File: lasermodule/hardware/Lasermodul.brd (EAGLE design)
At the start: 96 parts, among them IC1 MEGA8-AI

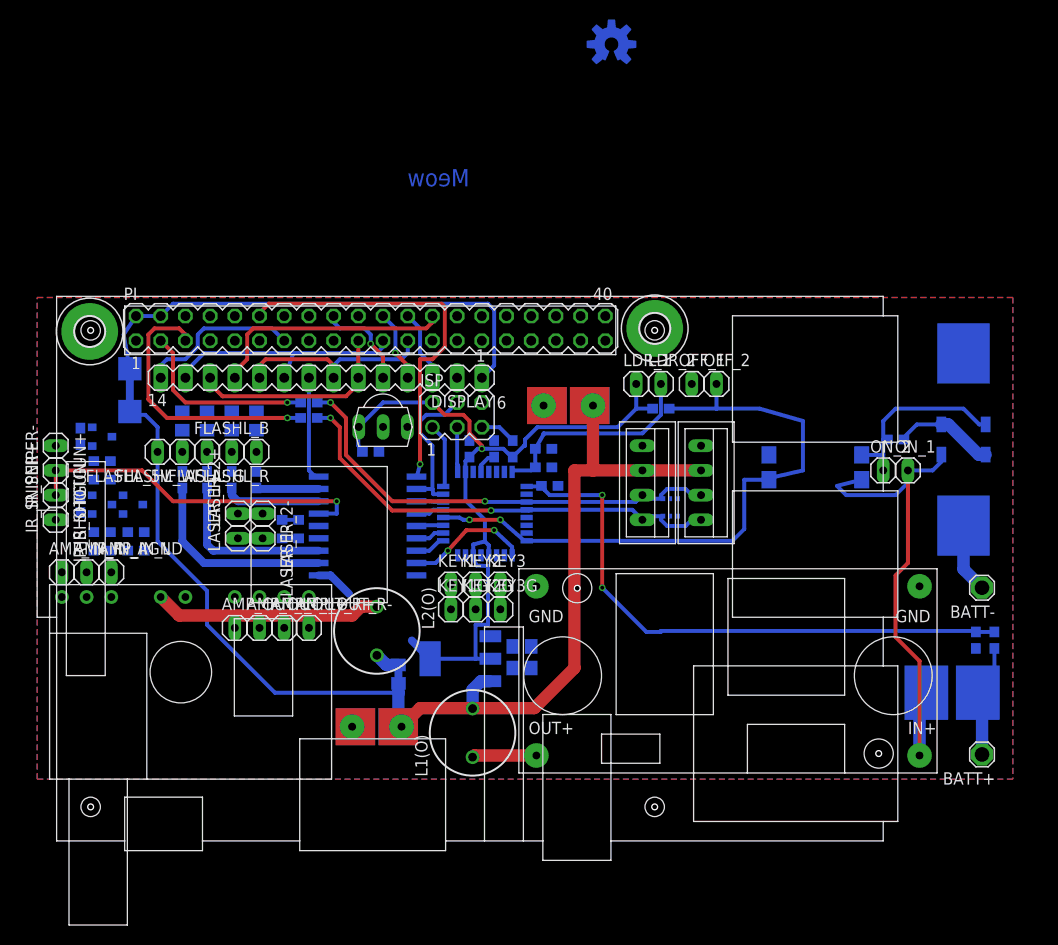
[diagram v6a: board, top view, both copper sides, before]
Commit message: routing and a bit case design
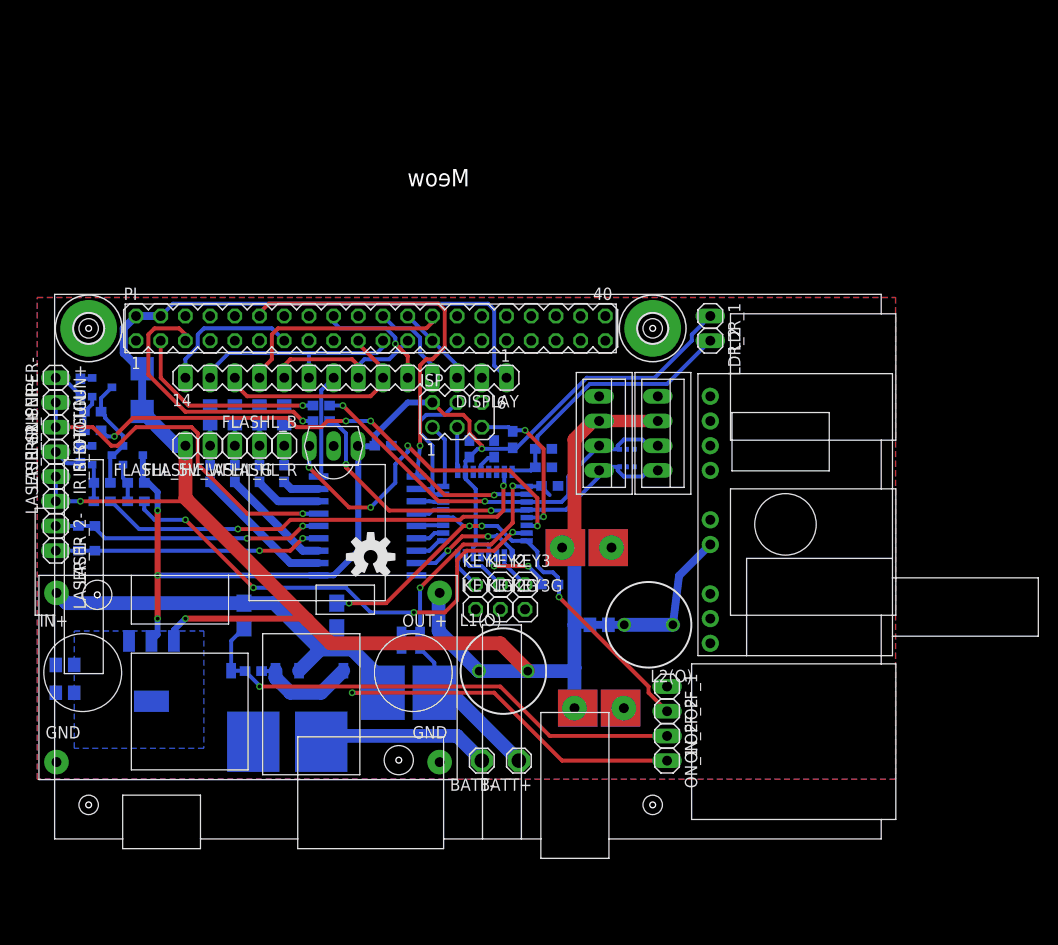
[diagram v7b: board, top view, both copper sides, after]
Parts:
- removed AMP_IN_AGND, AMP_IN_L, AMP_IN_R, AMP_OUT_L+, AMP_OUT_L-, AMP_OUT_R+, AMP_OUT_R-: (no value), wz:PIN-HEADER-1
- KEY1, KEY1G, KEY2, KEY2G, KEY3, KEY3G: device wz:PIN-HEADER-1 -> wz:PIN-HEADER-1_SMALL
- LOGO1: device wz:OSHW-LOGO-M -> SparkFun-Aesthetics:OSHW-LOGO-M
- moved ON 80.9 mm to (22.2, 6.35), turned to 180 degrees
- moved U$2 74.5 mm to (34.3, 46.4)
- moved R9 70.2 mm to (22.2, 11.1)
- moved REV 69.7 mm to (29.2, 6.35)
- moved U$4 67.1 mm to (67.9, 12.7), turned to 90 degrees
- moved R4 59.1 mm to (39.4, 14.3)
- moved R5 59.1 mm to (37.5, 14.3)
- moved LOGO1 58.2 mm to (34.3, 22.9)
- moved OK1 56.1 mm to (26.0, 16.8), turned to 270 degrees
- moved 2A_4A 55.9 mm to (41.9, 8.89)
- moved BATT- 54.4 mm to (45.7, 1.91)
- moved BATT+ 47.6 mm to (49.5, 1.91)
- moved C11 47.1 mm to (2.86, 8.89), turned to 0 degrees
- moved C2 47.0 mm to (2.86, 11.7), turned to 0 degrees
- moved ON_1 38.8 mm to (64.8, 1.91), turned to 270 degrees
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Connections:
- net +5V: now also C12.+A, C12.+B, C12.+C, C3.+A, C3.+B, C3.+C; no longer C12.1, C12.1B, C3.1, C3.1B
- net AMP_IN_AGND: no longer AMP_IN_AGND.1
- net AMP_IN_L: no longer AMP_IN_L.1
- net AMP_IN_R: no longer AMP_IN_R.1
- net AMP_OUT_L+: no longer AMP_OUT_L+.1
- net AMP_OUT_L-: no longer AMP_OUT_L-.1
- net AMP_OUT_R+: no longer AMP_OUT_R+.1
- net AMP_OUT_R-: no longer AMP_OUT_R-.1
- net GND: now also C12.-A, C12.-B, C12.-C, C3.-A, C3.-B, C3.-C; no longer C12.2, C12.2B, C3.2, C3.2B
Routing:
- net TX: track 0.00 -> 50.4 mm, vias 0 -> 4
- net I_IR_SHOTGUN: track 0.00 -> 48.7 mm, vias 0 -> 4
- net I_IR_SNIPER: track 0.00 -> 46.4 mm, vias 0 -> 2
- net +3V3: track 84.1 -> 122.5 mm, vias 1 -> 6
- net RX: track 0.00 -> 37.7 mm, vias 0 -> 4
- net BATT+_ADC: track 60.7 -> 27.3 mm
- net ONOFF_2: track 19.4 -> 52.7 mm, vias 0 -> 1
- net BATT+_FUSE: track 54.6 -> 80.2 mm, vias 0 -> 1
- net LASER_2: track 0.00 -> 24.2 mm, vias 0 -> 2
- net LASER_1: track 0.00 -> 23.5 mm, vias 0 -> 2
- net ONOFF: track 66.4 -> 50.5 mm, vias 2 -> 4
- net N$46: track 23.4 -> 9.63 mm
- net +5V: track 117.6 -> 130.1 mm, vias 0 -> 2
- net RESET: track 3.74 -> 16.1 mm, vias 0 -> 2
- net EASTEREGG_NET: track 0.00 -> 11.9 mm
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- added copper zone on layer 16, net +3V3

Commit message: routing
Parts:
- added SJ1: (no value), jumper:SJ
- moved R3(O) 2.54 mm to (57.8, 13.3)
- moved ON 0.95 mm to (21.3, 6.35)
- moved R9 0.95 mm to (21.3, 11.1)
- moved R5 0.79 mm to (36.7, 14.3)
- moved R16 0.71 mm to (52.7, 34.3)
- moved C4 0.65 mm to (52.7, 32.2)
- moved P-FET1 0.63 mm to (10.5, 33.3)
- moved P-FET2 0.63 mm to (7.30, 33.3)
- moved R4 0.63 mm to (38.7, 14.3)
- moved P-FET3 0.32 mm to (6.67, 40.6)
- moved R23 0.32 mm to (5.71, 38.1)
- moved R24 0.32 mm to (4.45, 40.6)
- moved R6 0.32 mm to (29.2, 38.7)
- moved R22 0.16 mm to (5.71, 36.0)
- moved R21 0.16 mm to (4.60, 33.3)
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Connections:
- net +5V: now also C12.+, C3.+; no longer C12.+A, C12.+B, C12.+C, C3.+A, C3.+B, C3.+C
- net AMP_IN_AGND: now also SJ1.2
- net GND: now also C12.-, C3.-, SJ1.1; no longer C12.-A, C12.-B, C12.-C, C3.-A, C3.-B, C3.-C
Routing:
- net I_BACKLIGHT: track 38.6 -> 44.1 mm
- net RX: track 37.7 -> 32.9 mm, vias 4 -> 3
- net N$45: track 1.63 -> 4.15 mm
- net AMP_IN_AGND: track 0.00 -> 2.41 mm
- net GND: track 0.00 -> 2.34 mm, vias 0 -> 92
- net ONOFF_2: track 52.7 -> 54.6 mm
- net LCD_DC: track 12.3 -> 10.6 mm
- net ONOFF: track 50.5 -> 49.4 mm
- net LCD_CS: track 8.45 -> 9.57 mm
- net EASTEREGG_NET: track 11.9 -> 12.8 mm
- net +3V3: track 122.5 -> 123.4 mm
- net N$46: track 9.63 -> 8.73 mm
- net BATT+_ADC: track 27.3 -> 26.5 mm
- net SCL_BUS: track 43.5 -> 44.3 mm
- net LCD_SCK: track 18.1 -> 17.3 mm
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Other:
- board outline added: 88.3 x 49.5 mm
